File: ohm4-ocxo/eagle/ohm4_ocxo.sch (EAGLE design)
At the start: 17 parts, among them U1 TPS73650, U2 TLV1117, X1 BU-SMA-V, X2 U.FL

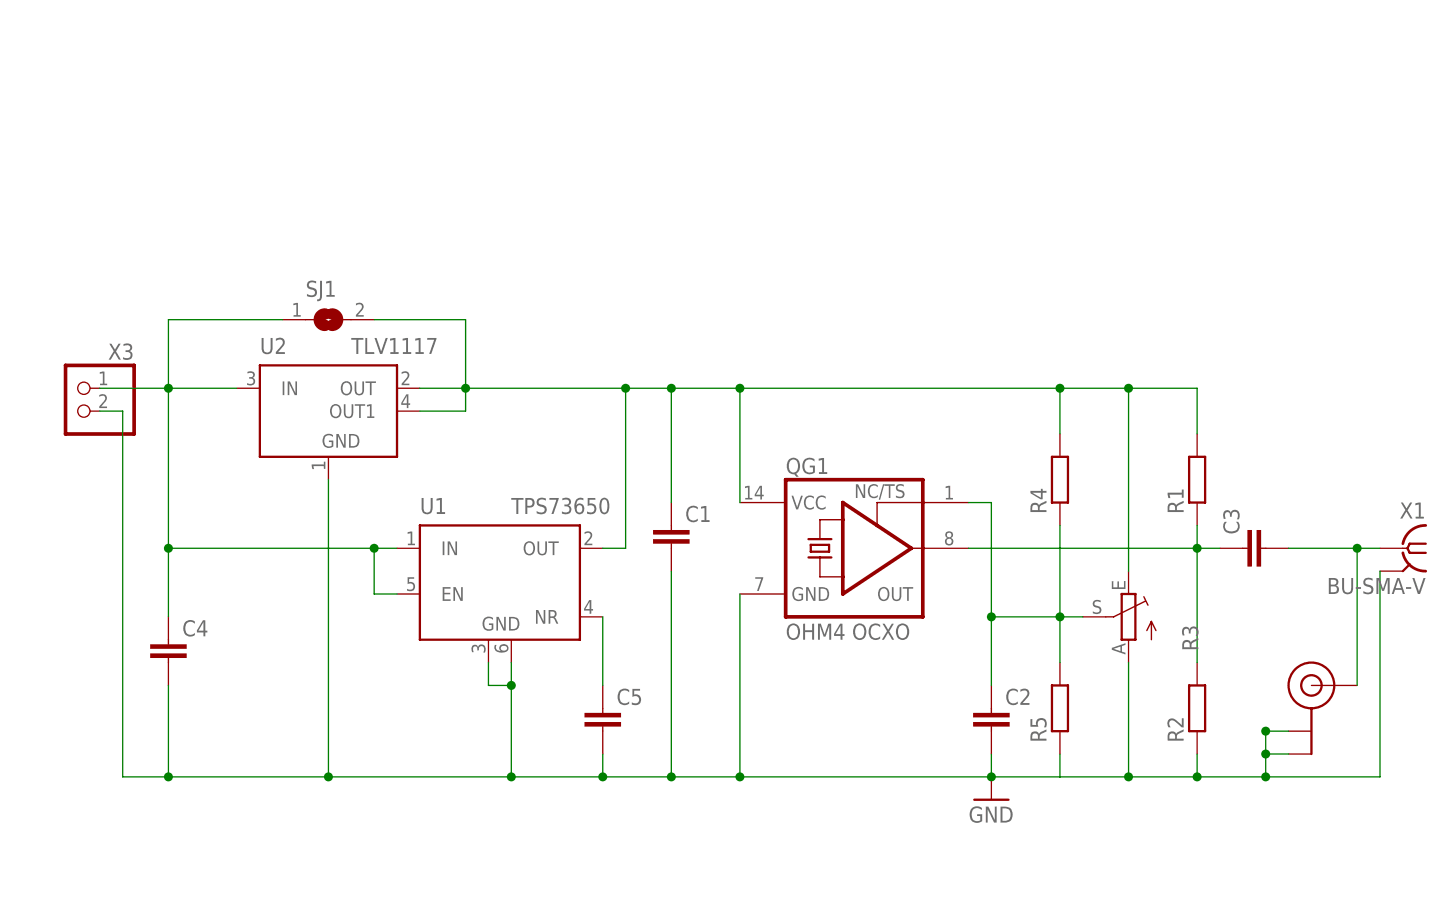
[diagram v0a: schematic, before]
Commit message: update to version with PLL ic onboard
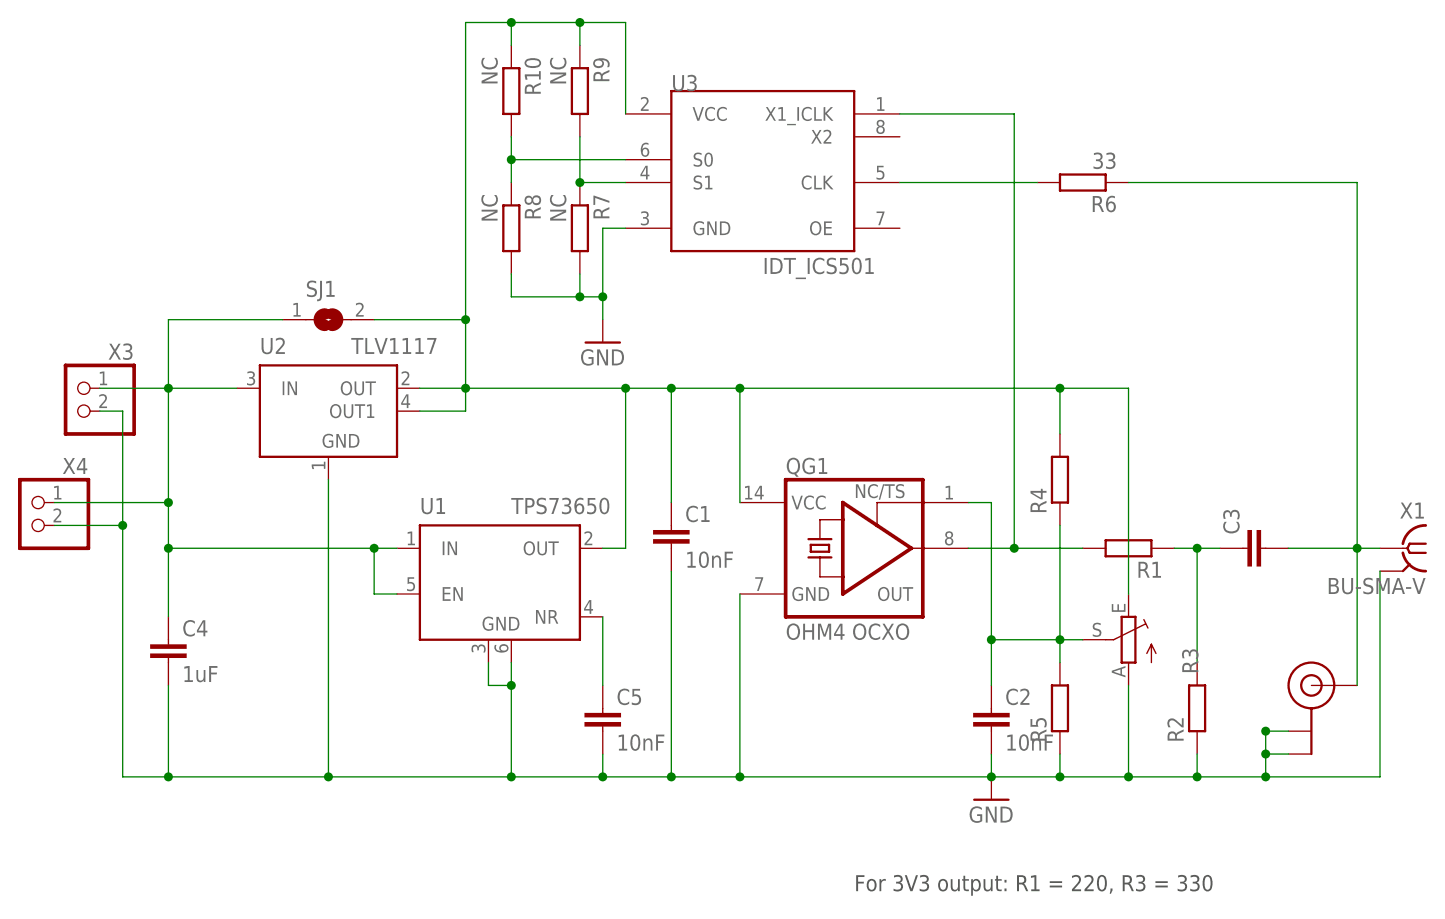
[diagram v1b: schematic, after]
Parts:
- added R10, R7, R8, R9: NC, rcl:R-EU_R0603
- added R6: 33, rcl:R-EU_R0603
- added U3: IDT_ICS501, laforge:IDT_ICS501
- added X4: (no value), pinhead:PINHD-1X2
- C1, C2, C5: value (none) -> 10nF
- C4: value (none) -> 1uF
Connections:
- new net N$6: QG1.OUT, R1.2, U3.X1_ICLK
- new net N$7: R6.2, U3.CLK
- new net N$8: R7.1, R9.2, U3.S1
- new net N$9: R10.2, R8.1, U3.S0
- net 5V: now also R10.1, R9.1, U3.VCC; no longer R1.2
- net GND: now also R7.2, R8.2, U3.GND, X4.2
- net N$1: no longer QG1.OUT
- net N$3: now also X4.1
- net N$4: now also R6.1
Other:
- note added: "For 3V3 output: R1 = 220, R3 = 330"
- moved on the sheet: R1, R3

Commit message: update OHM4 OCXO, preliminary v3
 * use new LDO (single LDO with range up to 12V input)
 * add U.FL clock input (instead of OCXO as source)
 * no parallel, but series resistors to trimmer
 * allow output of PLL to be fed through resistive divider
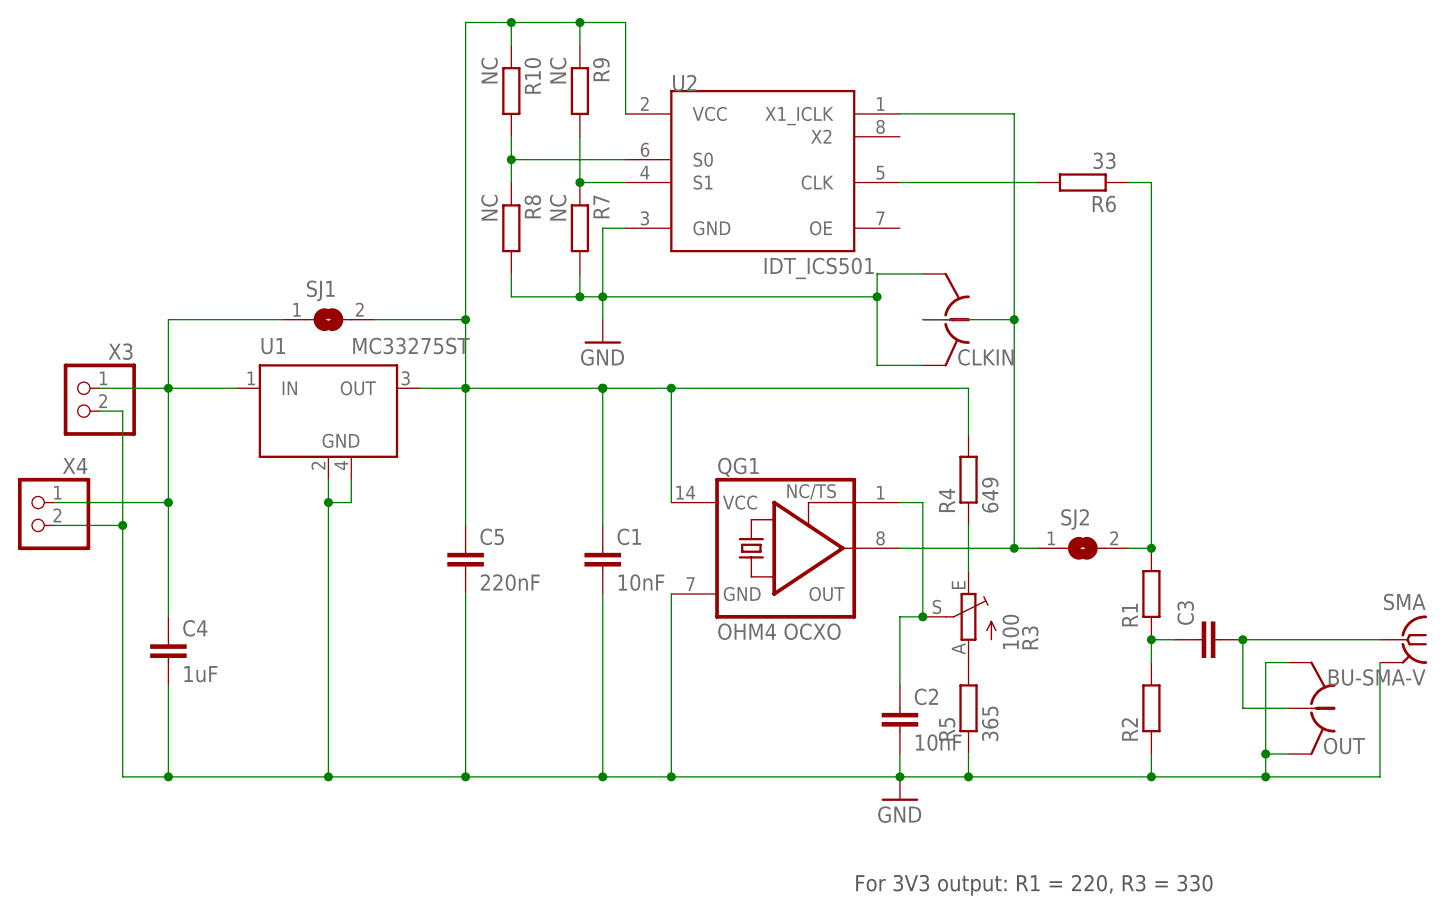
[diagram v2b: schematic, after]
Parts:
- removed U3: IDT_ICS501, laforge:IDT_ICS501
- removed X1: BU-SMA-V, con-coax:BU-SMA-V
- removed X2: U.FL, SparkFun-Connectors:U.FL
- added CLKIN, OUT: (no value), laforge:HRS_UFL
- added SJ2: (no value), jumper:SJ
- added SMA: BU-SMA-V, con-coax:BU-SMA-V
- C5: value 10nF -> 220nF
- R3: value (none) -> 100
- R4: value (none) -> 649
- R5: value (none) -> 365
- U1: value TPS73650 -> MC33275ST; device laforge:TPS736XX -> laforge:MC33275ST
- U2: value TLV1117 -> IDT_ICS501; device laforge:TLV1117 -> laforge:IDT_ICS501
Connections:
- removed net 5V: C1.1, QG1.VCC, R10.1, R3.E, R4.2, R9.1, SJ1.2, U1.OUT, U2.OUT, U2.OUT1, U3.VCC
- removed net N$2: C5.1, U1.NR
- new net N$10: R3.A, R5.2
- new net N$11: R3.E, R4.1
- new net N$12: C3.2, OUT.1, SMAG$1.1
- new net U1: C1.1, C5.1, QG1.VCC, R10.1, R4.2, R9.1, SJ1.2, U1.OUT, U2.VCC
- net GND: now also CLKIN.GND@1, CLKIN.GND@2, OUT.GND@1, OUT.GND@2, SMAG$1.GND; no longer R3.A, U3.GND, X1G$1.GND, X2.GND@0, X2.GND@1
- net N$3: no longer U1.EN, U2.IN
- net N$4: now also R1.2, SJ2.2; no longer C3.2, X1G$1.1, X2.SIGNAL
- net N$5: no longer R4.1, R5.2
- net N$6: now also CLKIN.1, SJ2.1, U2.X1_ICLK; no longer R1.2, U3.X1_ICLK
- net N$7: now also U2.CLK; no longer U3.CLK
- net N$8: now also U2.S1; no longer U3.S1
- net N$9: now also U2.S0; no longer U3.S0
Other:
- moved on the sheet: C1, C2, C3, C5, QG1, R1, R2, R3, R4, R5

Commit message: final v3 as it goes in pcb production
* smash components and move labels to where they can be read
* add indication of + / GND to X3/X4
* re-route some traces to ensure sufficient distance between them
* make all traces 0.508 mm wide, even signal traces.
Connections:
- net U1 renamed VCC
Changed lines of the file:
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@@
 </segment>
 </net>
-<net name="U1" class="1">
+<net name="VCC" class="1">
 <segment>
 <pinref part="QG1" gate="G$1" pin="VCC"/>
